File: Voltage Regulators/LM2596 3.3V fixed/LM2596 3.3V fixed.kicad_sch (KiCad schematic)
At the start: 5 parts, among them U1 LM2596S-3.3V

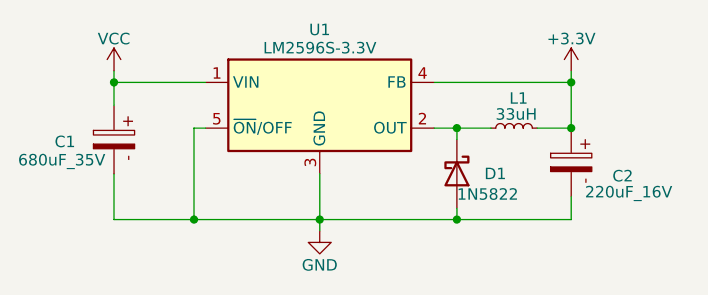
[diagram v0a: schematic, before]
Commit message: Edited 1N5822 to 1N5824
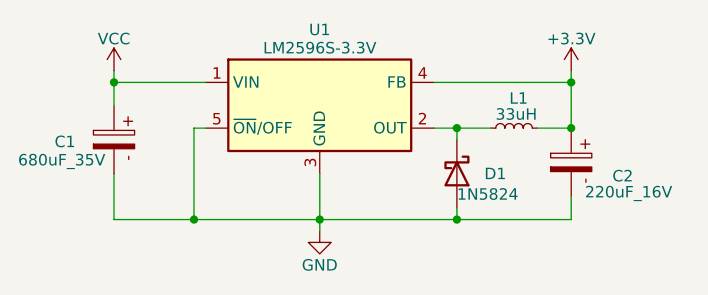
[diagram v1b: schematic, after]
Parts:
- D1: value 1N5822 -> 1N5824
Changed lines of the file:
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@@
 			)
 		)
-		(property "Value" "1N5822"
+		(property "Value" "1N5824"
 			(at 165.1 111.506 90)
 			(effects
